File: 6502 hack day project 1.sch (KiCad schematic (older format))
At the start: 6 parts, among them J1 USB_B_Micro, SW1 SW_SPST, U1 MAX707

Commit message: free-run.
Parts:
- added C?: 0.1 uF, symbol Device:C
- added C?: 4.7 uF, symbol Device:CP
- added R1, R2, R3, R4: 3.3k, symbol Device:R
- added R10, R6, R7, R8, R9: 4.7k, symbol Device:R
- added R5: 47, symbol Device:R
- added U2: W65C02SxP, symbol 65xx:W65C02SxP
- gave numbers to parts that had none: 1
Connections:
- wire segments 19 -> 64
- no-connect marks 9 -> 30
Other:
- moved on the sheet: C1, C2, SW1, U1, X1

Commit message: adding flash and flash firmware.
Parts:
- removed R10, R6, R7, R8, R9: 4.7k, symbol Device:R
- removed R5: 47, symbol Device:R
- added C5: 0.1 uF, symbol Device:C
- added U3: Am29F010, symbol My-CPU-Stuff:Am29F010
- gave numbers to parts that had none: 2
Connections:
- net labels added: D0, D1, D2, D3, D4, D5, D6, D7
- wire segments 64 -> 96
- no-connect marks 30 -> 17

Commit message: update schematic.
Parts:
- removed J1: USB_B_Micro, symbol Connector:USB_B_Micro
- added C1: CP, symbol Device:CP
- added C2, C7, C9: C, symbol Device:C
- added D1: 1N4148, Diode_THT:D_DO-35_SOD27_P7.62mm_Horizontal, symbol Diode:1N4148
- added J1: Barrel_Jack_MountingPin, symbol Connector:Barrel_Jack_MountingPin
- added J2: Conn_02x02_Odd_Even, symbol Connector_Generic:Conn_02x02_Odd_Even
- added J3: Conn_01x06, symbol Connector_Generic:Conn_01x06
- added R1: 10k, symbol Device:R
- added R2: 47k, symbol Device:R
- added R3, R4: R, symbol Device:R
- added SW1: SW_SPST, symbol Switch:SW_SPST
- added U1: LM7805_TO220, Package_TO_SOT_THT:TO-220-3_Vertical, symbol Regulator_Linear:LM7805_TO220
- added U2: 74HC14, symbol 74xx:74HC14
- added U4: 74HC00, symbol 74xx:74HC00
- added U6: 6551, symbol 65xx:6551
- added X2: CXO_DIP8, Oscillator:Oscillator_DIP-8, symbol Oscillator:CXO_DIP8
- renumbered C1 to C4, C2 to C5, C4 to C6, C5 to C8, R1 to R5, R2 to R6, R3 to R7, R4 to R8, SW1 to SW2, U1 to U3, U2 to U5, U3 to U7
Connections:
- net labels added: CTS, DTR, RX, TX, VIO
- wire segments 96 -> 196
- no-connect marks 17 -> 20
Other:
- moved on the sheet: C3, C4, C5, C6, C8, R5, R6, R7, R8, SW2, U3, U5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

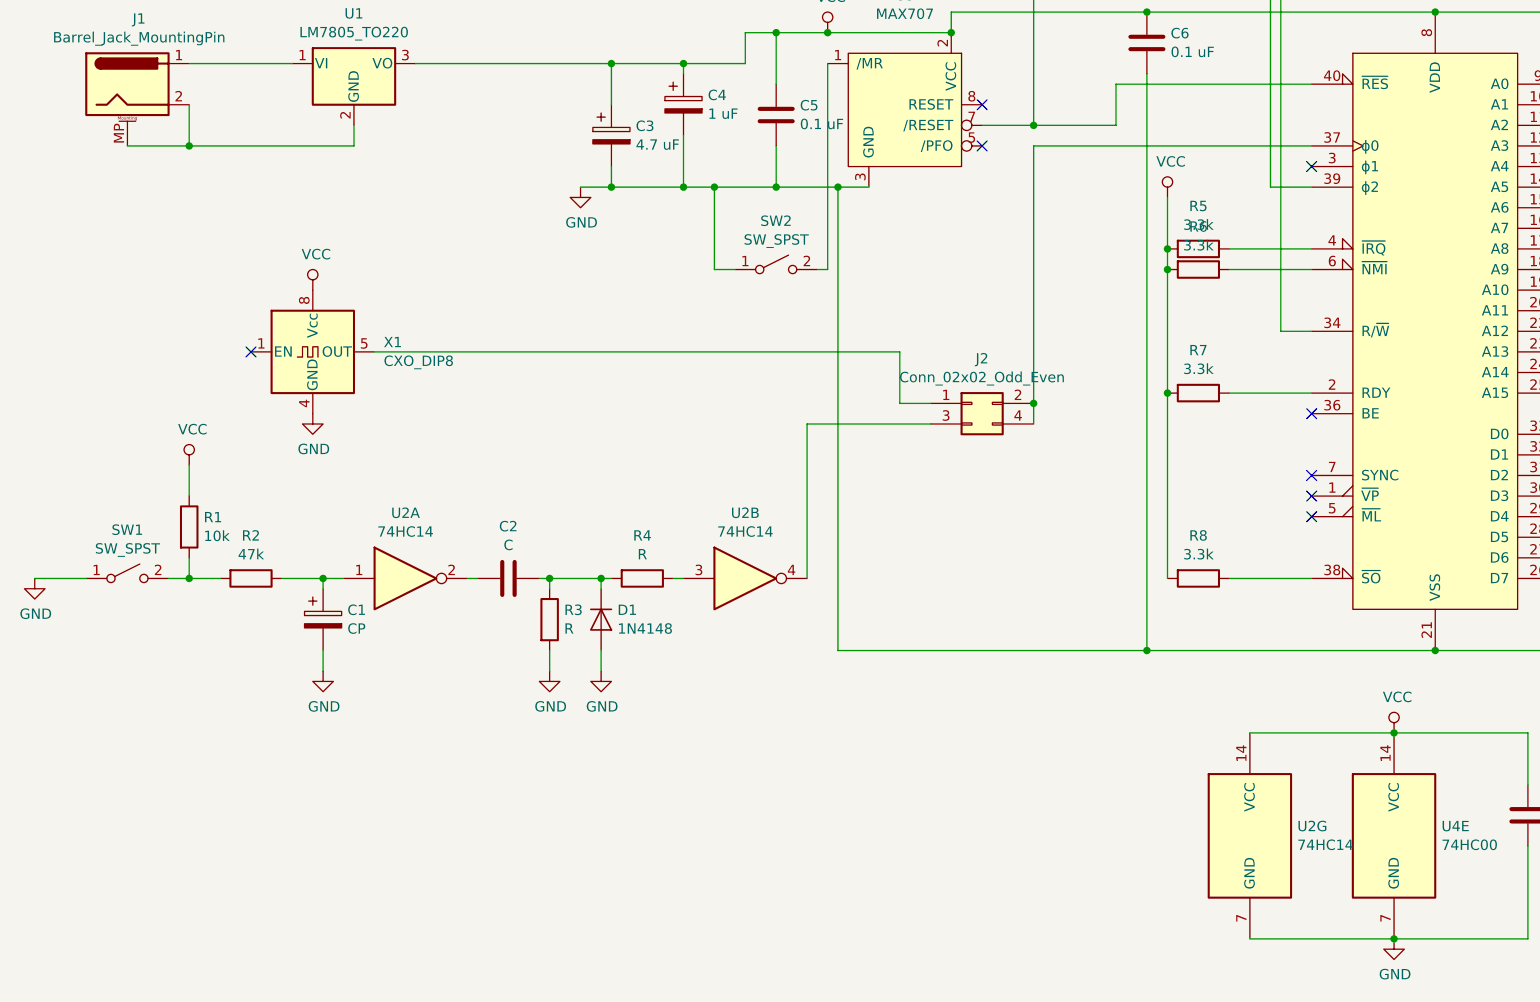
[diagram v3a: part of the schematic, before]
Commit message: got the serial port working
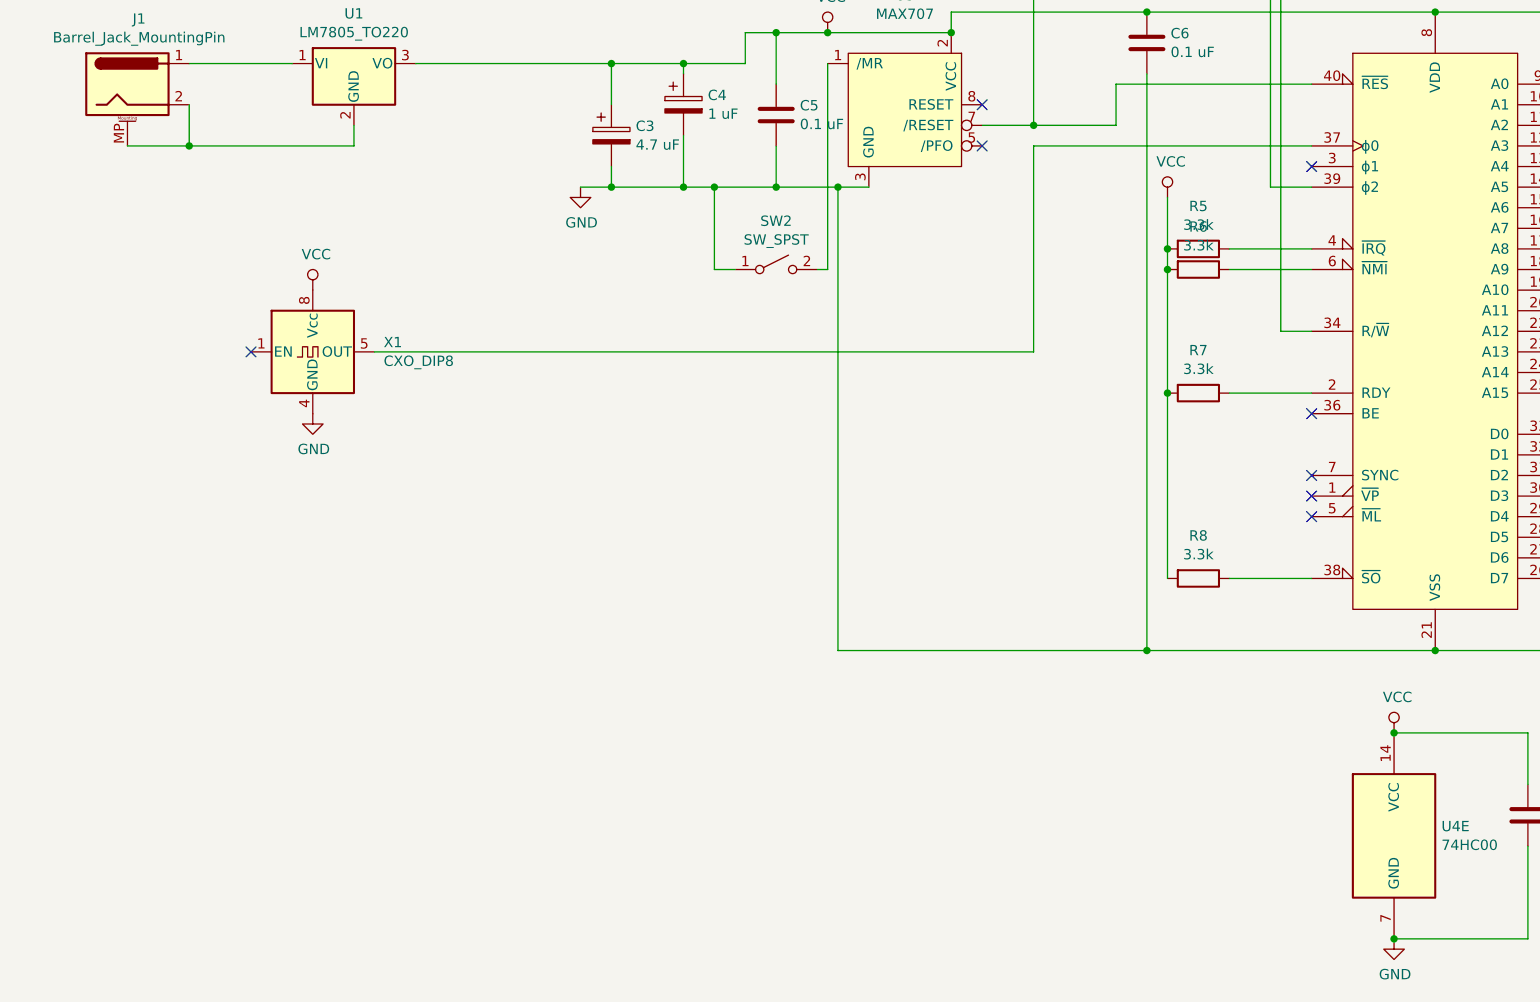
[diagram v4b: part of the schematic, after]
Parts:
- removed C1: CP, symbol Device:CP
- removed C2: C, symbol Device:C
- removed D1: 1N4148, Diode_THT:D_DO-35_SOD27_P7.62mm_Horizontal, symbol Diode:1N4148
- removed J2: Conn_02x02_Odd_Even, symbol Connector_Generic:Conn_02x02_Odd_Even
- removed R1: 10k, symbol Device:R
- removed R2: 47k, symbol Device:R
- removed R3, R4: R, symbol Device:R
- removed SW1: SW_SPST, symbol Switch:SW_SPST
- removed U2: 74HC14, symbol 74xx:74HC14
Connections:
- net at X1.5 (OUT): now also U5.37 (ϕ0)

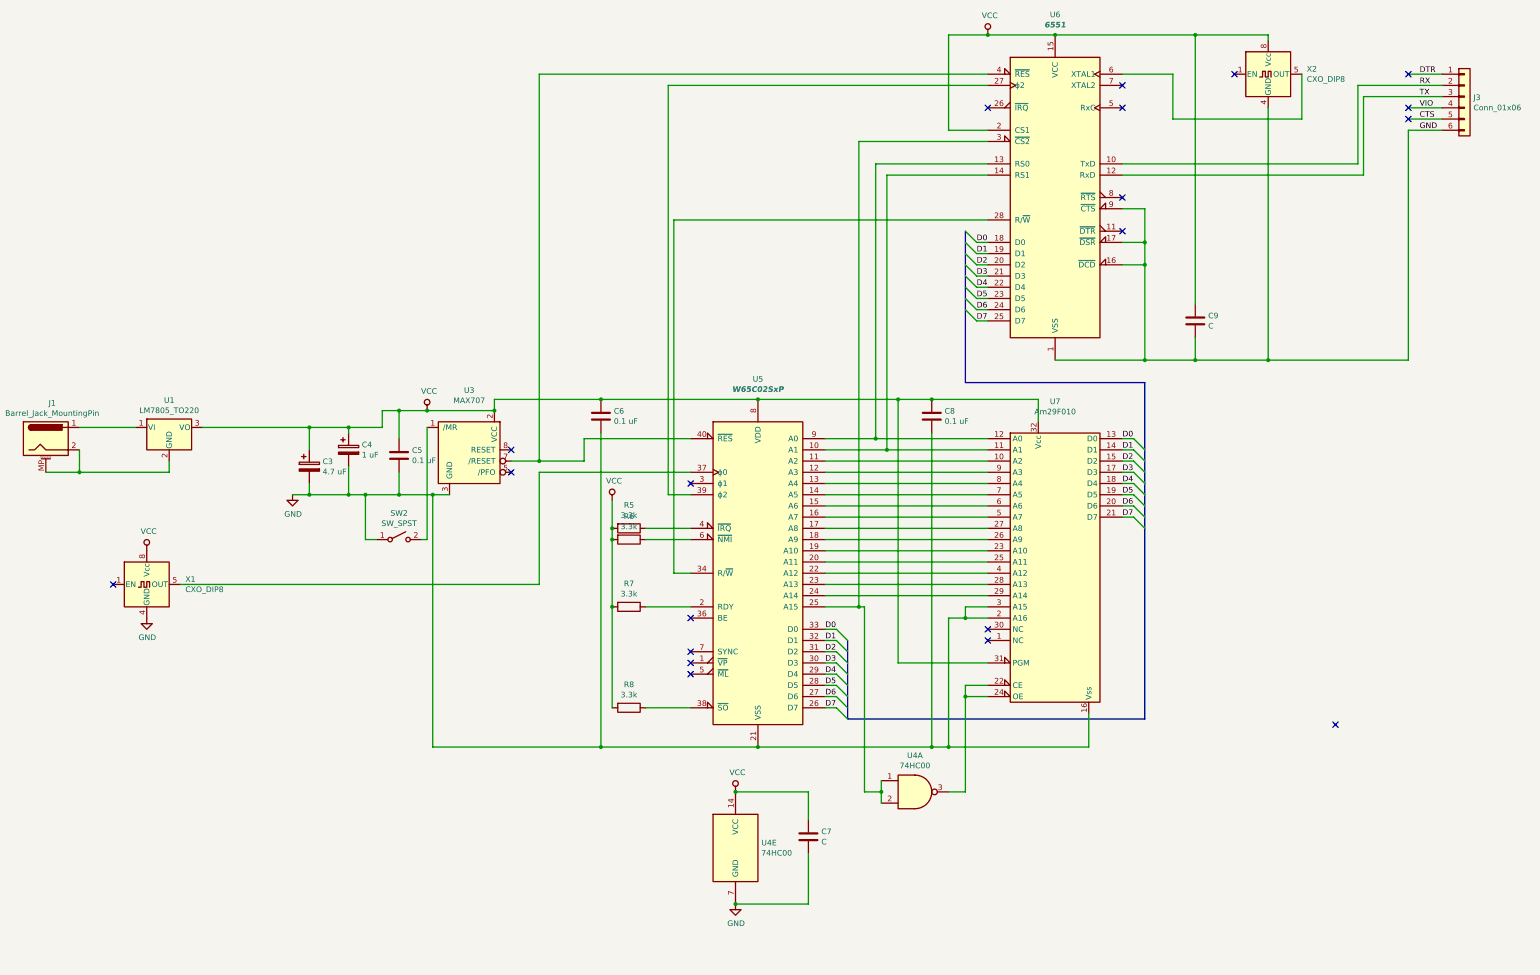
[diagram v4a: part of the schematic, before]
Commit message: Breaking out the lines for RAM and IO.
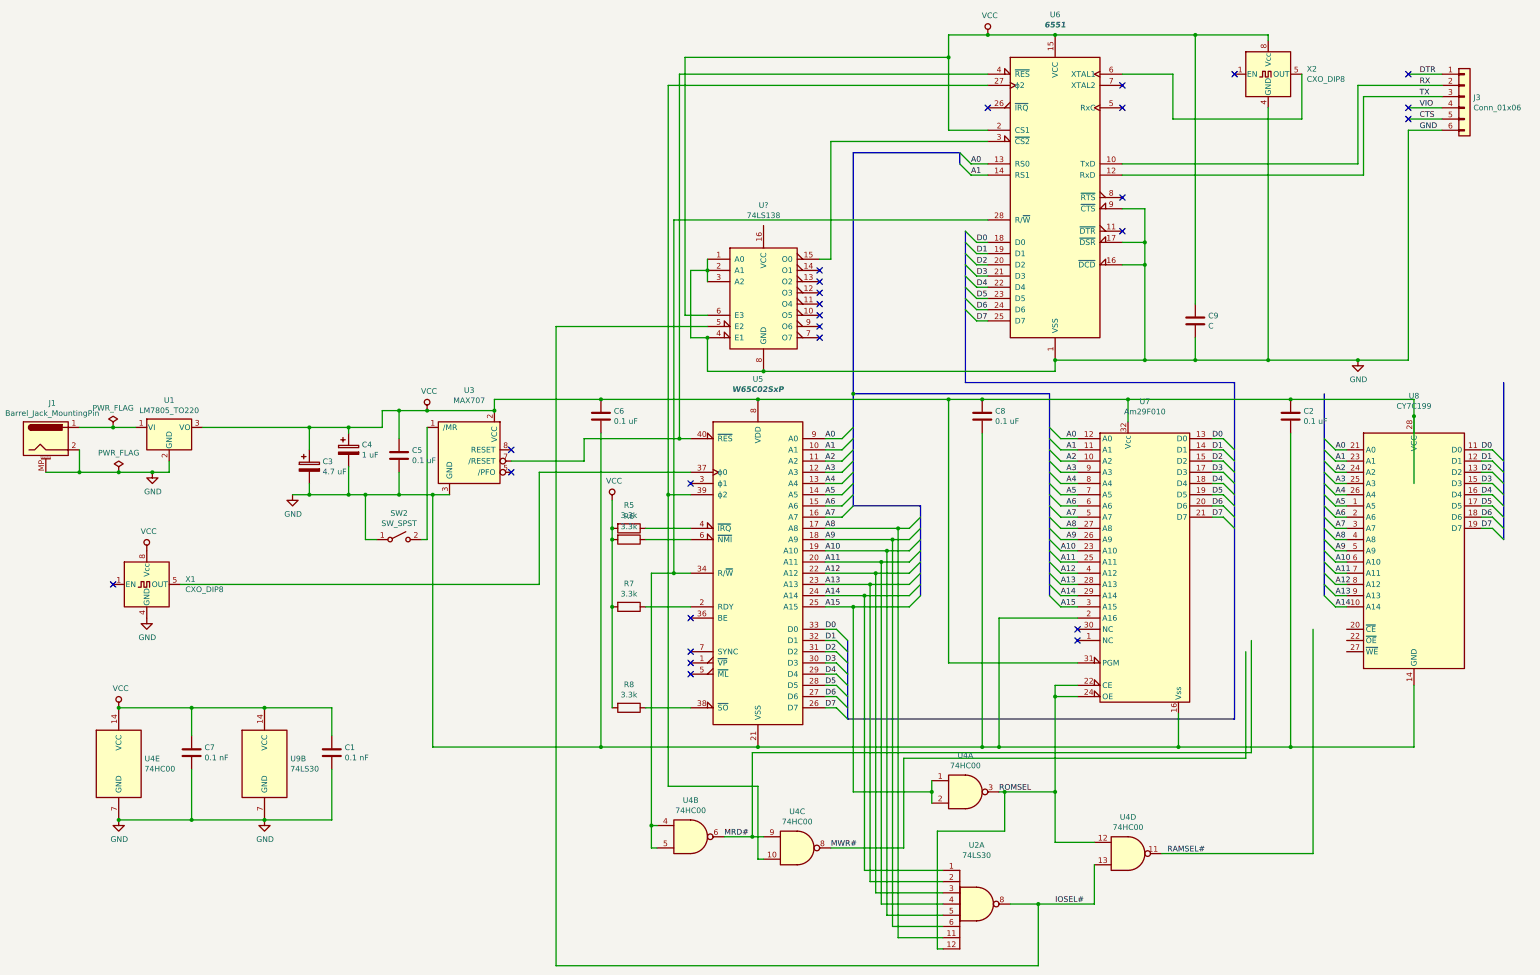
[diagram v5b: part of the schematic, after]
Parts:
- added C1: 0.1 nF, symbol Device:C
- added C2: 0.1 uF, symbol Device:C
- added U2, U9: 74LS30, symbol 74xx:74LS30
- added unit 2 of U4
- added unit 3 of U4
- added unit 4 of U4
- added U8: CY7C199, symbol Memory_RAM:CY7C199
- added U?: 74LS138, symbol 74xx:74LS138
- C7: value C -> 0.1 nF
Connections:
- net D0: now also U8.11 (D0)
- net D1: now also U8.12 (D1)
- net D2: now also U8.13 (D2)
- net D3: now also U8.15 (D3)
- net D4: now also U8.16 (D4)
- net D5: now also U8.17 (D5)
- net D6: now also U8.18 (D6)
- net D7: now also U8.19 (D7)
- net GND: now also J1.2, J1.MP (MountPin), U1.2 (GND), C1.2, C2.2, U8.14 (GND), U9.7 (GND), U?.1 (A0), U?.2 (A1), U?.3 (A2), U?.4 (E1), U?.8 (GND); no longer U7.3 (A15)
- net VCC: now also C1.1, C2.1, U8.28 (VCC), U9.14 (VCC), U?.6 (E3)
- net A1: now reaches U5.10 (A1), U6.14 (RS1), U7.11 (A1)
- net A1: now also U8.23 (A1)
- net A2: now reaches U5.11 (A2), U7.10 (A2)
- net A2: now also U8.24 (A2)
- net A3: now reaches U5.12 (A3), U7.9 (A3)
- net A3: now also U8.25 (A3)
- net A4: now reaches U5.13 (A4), U7.8 (A4)
- net A4: now also U8.26 (A4)
- net A5: now reaches U5.14 (A5), U7.7 (A5)
- net A5: now also U8.1 (A5)
- net A6: now reaches U5.15 (A6), U7.6 (A6)
- net A6: now also U8.2 (A6)
- net A7: now reaches U5.16 (A7), U7.5 (A7)
- net A7: now also U8.3 (A7)
- net A8: now reaches U5.17 (A8), U7.27 (A8)
- net A8: now also U2.11, U8.4 (A8)
- net A9: now reaches U5.18 (A9), U7.26 (A9)
- net A9: now also U2.6, U8.5 (A9)
- net A10: now reaches U5.19 (A10), U7.23 (A10)
- net A10: now also U2.5, U8.6 (A10)
- net A11: now reaches U5.20 (A11), U7.25 (A11)
- net A11: now also U2.4, U8.7 (A11)
- net A12: now reaches U5.22 (A12), U7.4 (A12)
- net A12: now also U2.3, U8.8 (A12)
- net A13: now reaches U5.23 (A13), U7.28 (A13)
- net A13: now also U2.2, U8.9 (A13)
- net A14: now reaches U5.24 (A14), U7.29 (A14)
- net A14: now also U2.1, U8.10 (A14)
- net A15: now reaches U4.1, U4.2, U5.25 (A15)
- net A15: now also U7.3 (A15); no longer U6.3 (~CS2)
- net at U5.34 (R/~W), U6.28 (R/~W): now also U4.4, U4.5
- net at U5.39 (ϕ2), U6.27 (ϕ2): now also U4.10
- net A0: now reaches U5.9 (A0), U6.13 (RS0), U7.12 (A0)
- net A0: now also U8.21 (A0)
- net ROMSEL: now reaches U4.3, U7.22 (CE), U7.24 (OE)
- net ROMSEL: now also U2.12, U4.12
- new net: U6.3 (~CS2), U?.15 (O0)
- new net IOSEL#: U2.8, U4.13, U?.5 (E2)
- new net MRD#: U4.6, U4.9
- new net MWR#: U4.8
- new net RAMSEL#: U4.11
- no-connect marks 20 -> 26
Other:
- moved on the sheet: C7, C8, U4A, U4E, U7
